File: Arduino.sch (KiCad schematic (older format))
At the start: 16 parts

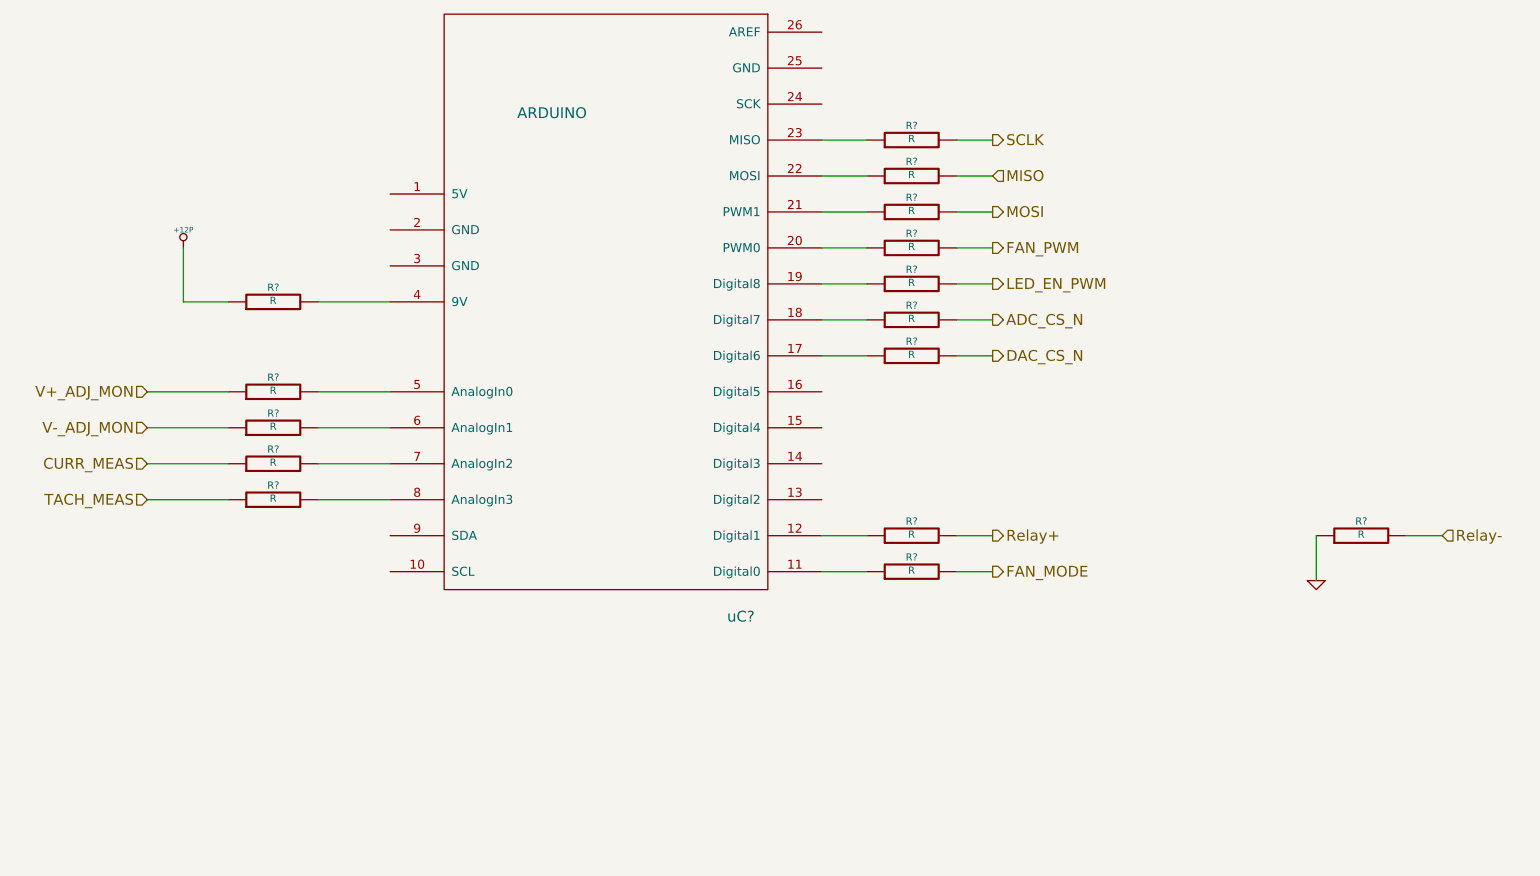
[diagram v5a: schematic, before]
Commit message: 5.3 Video 1/2 Associating and Placing the Relay Module
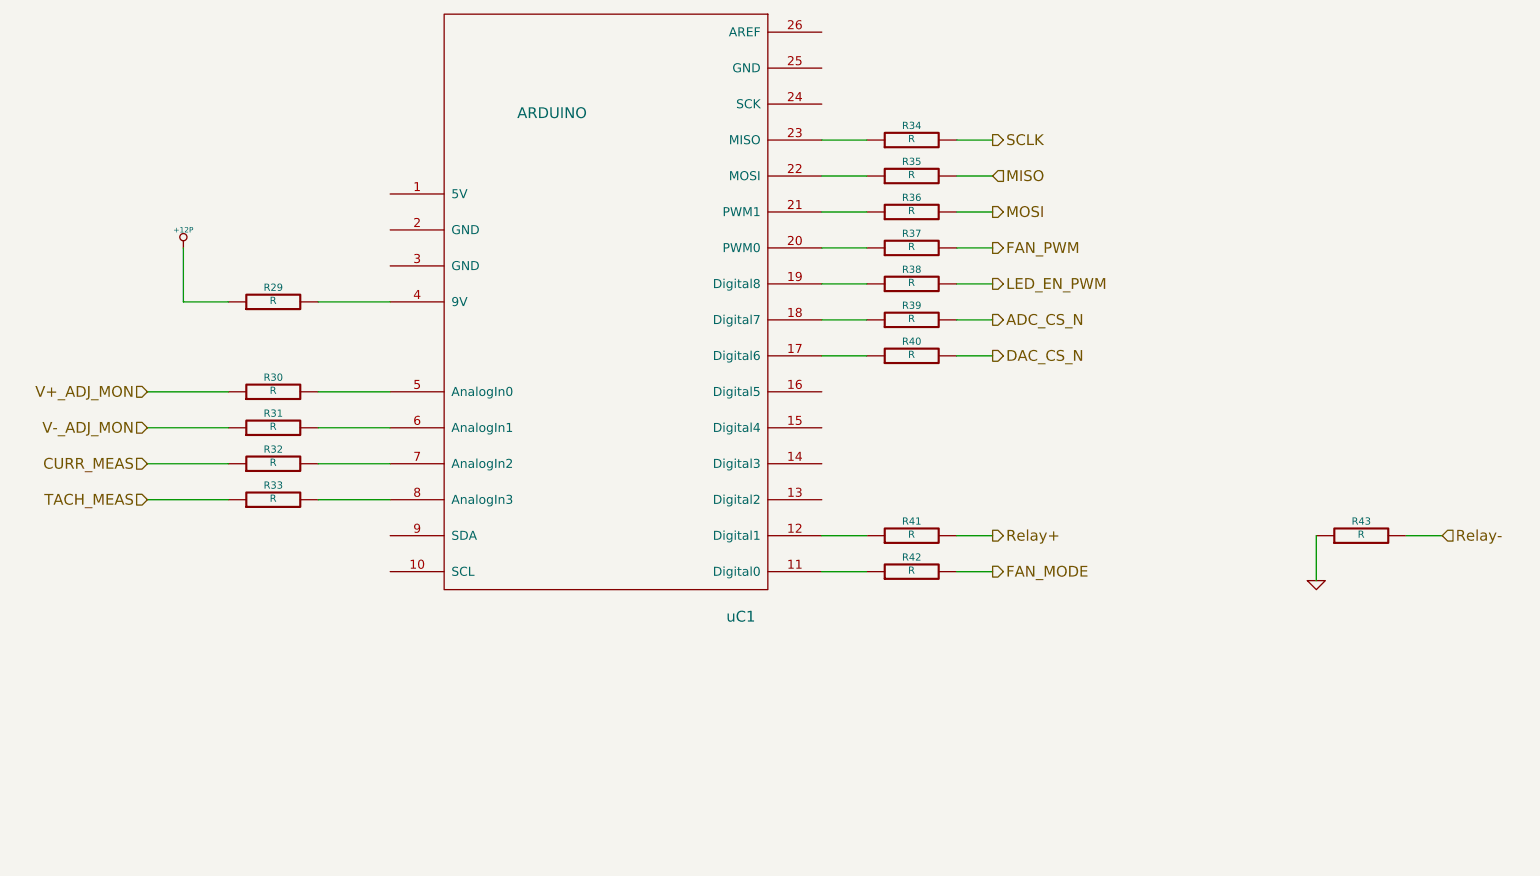
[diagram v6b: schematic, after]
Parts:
- gave numbers to parts that had none: 16
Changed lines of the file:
@@
 Sheet 9 9
 Title ""
-Date "13 feb 2014"
+Date "19 feb 2014"
 Rev ""
 Comp ""
@@
 TACH_MEAS
 $Comp
-L R R?
+L R R30
 U 1 1 52F8F2D4
 P 2100 4000
-F 0 "R?" V 2180 4000 40  0000 C CNN
+F 0 "R30" V 2180 4000 40  0000 C CNN
 F 1 "R" V 2107 4001 40  0000 C CNN
 F 2 "~" V 2030 4000 30  0000 C CNN
@@
 $EndComp
 $Comp
-L R R?
+L R R31
 U 1 1 52F8F2E1
 P 2100 4200
-F 0 "R?" V 2180 4200 40  0000 C CNN
+F 0 "R31" V 2180 4200 40  0000 C CNN
 F 1 "R" V 2107 4201 40  0000 C CNN
 F 2 "~" V 2030 4200 30  0000 C CNN
@@
 $EndComp
 $Comp
-L R R?
+L R R32
 U 1 1 52F8F2E7
 P 2100 4400
-F 0 "R?" V 2180 4400 40  0000 C CNN
+F 0 "R32" V 2180 4400 40  0000 C CNN
 F 1 "R" V 2107 4401 40  0000 C CNN
 F 2 "~" V 2030 4400 30  0000 C CNN
@@
 $EndComp
 $Comp
-L R R?
+L R R33
 U 1 1 52F8F2F7
 P 2100 4600
-F 0 "R?" V 2180 4600 40  0000 C CNN
+F 0 "R33" V 2180 4600 40  0000 C CNN
 F 1 "R" V 2107 4601 40  0000 C CNN
 F 2 "~" V 2030 4600 30  0000 C CNN
@@
 	2750 4600 2350 4600
 $Comp
-L R R?
+L R R34
 U 1 1 52F8F30B
 P 5650 2600
-F 0 "R?" V 5730 2600 40  0000 C CNN
+F 0 "R34" V 5730 2600 40  0000 C CNN
 F 1 "R" V 5657 2601 40  0000 C CNN
 F 2 "~" V 5580 2600 30  0000 C CNN
@@
 $EndComp
 $Comp
-L R R?
+L R R35
 U 1 1 52F8F318
 P 5650 2800
-F 0 "R?" V 5730 2800 40  0000 C CNN
+F 0 "R35" V 5730 2800 40  0000 C CNN
 F 1 "R" V 5657 2801 40  0000 C CNN
 F 2 "~" V 5580 2800 30  0000 C CNN
@@
 $EndComp
 $Comp
-L R R?
+L R R36
 U 1 1 52F8F31E
 P 5650 3000
-F 0 "R?" V 5730 3000 40  0000 C CNN
+F 0 "R36" V 5730 3000 40  0000 C CNN
 F 1 "R" V 5657 3001 40  0000 C CNN
 F 2 "~" V 5580 3000 30  0000 C CNN
@@
 $EndComp
 $Comp
-L R R?
+L R R39
 U 1 1 52F8F324
 P 5650 3600
-F 0 "R?" V 5730 3600 40  0000 C CNN
+F 0 "R39" V 5730 3600 40  0000 C CNN
 F 1 "R" V 5657 3601 40  0000 C CNN
 F 2 "~" V 5580 3600 30  0000 C CNN
@@
 $EndComp
 $Comp
-L R R?
+L R R41
 U 1 1 52F8F32A
 P 5650 4800
-F 0 "R?" V 5730 4800 40  0000 C CNN
+F 0 "R41" V 5730 4800 40  0000 C CNN
 F 1 "R" V 5657 4801 40  0000 C CNN
 F 2 "~" V 5580 4800 30  0000 C CNN
@@
 $EndComp
 $Comp
-L R R?
+L R R37
 U 1 1 52F8F330
 P 5650 3200
-F 0 "R?" V 5730 3200 40  0000 C CNN
+F 0 "R37" V 5730 3200 40  0000 C CNN
 F 1 "R" V 5657 3201 40  0000 C CNN
 F 2 "~" V 5580 3200 30  0000 C CNN
@@
 Relay-
 $Comp
-L GND #PWR?
+L GND #PWR048
 U 1 1 52F8F33B
 P 7900 5050
-F 0 "#PWR?" H 7900 5050 30  0001 C CNN
+F 0 "#PWR048" H 7900 5050 30  0001 C CNN
 F 1 "GND" H 7900 4980 30  0001 C CNN
 F 2 "" H 7900 5050 60  0000 C CNN
@@
 $EndComp
 $Comp
-L R R?
+L R R43
 U 1 1 52F8F34C
 P 8150 4800
-F 0 "R?" V 8230 4800 40  0000 C CNN
+F 0 "R43" V 8230 4800 40  0000 C CNN
 F 1 "R" V 8157 4801 40  0000 C CNN
 F 2 "~" V 8080 4800 30  0000 C CNN
@@
 DAC_CS_N
 $Comp
-L R R?
+L R R40
 U 1 1 52F844DD
 P 5650 3800
-F 0 "R?" V 5730 3800 40  0000 C CNN
+F 0 "R40" V 5730 3800 40  0000 C CNN
 F 1 "R" V 5657 3801 40  0000 C CNN
 F 2 "~" V 5580 3800 30  0000 C CNN
@@
 LED_EN_PWM
 $Comp
-L R R?
+L R R38
 U 1 1 52F844E8
 P 5650 3400
-F 0 "R?" V 5730 3400 40  0000 C CNN
+F 0 "R38" V 5730 3400 40  0000 C CNN
 F 1 "R" V 5657 3401 40  0000 C CNN
 F 2 "~" V 5580 3400 30  0000 C CNN
@@
 FAN_MODE
 $Comp
-L R R?
+L R R42
 U 1 1 52F897E0
 P 5650 5000
-F 0 "R?" V 5730 5000 40  0000 C CNN
+F 0 "R42" V 5730 5000 40  0000 C CNN
 F 1 "R" V 5657 5001 40  0000 C CNN
 F 2 "~" V 5580 5000 30  0000 C CNN
@@
 	5900 5000 6100 5000
 $Comp
-L R R?
+L R R29
 U 1 1 52F897E9
 P 2100 3500
-F 0 "R?" V 2180 3500 40  0000 C CNN
+F 0 "R29" V 2180 3500 40  0000 C CNN
 F 1 "R" V 2107 3501 40  0000 C CNN
 F 2 "~" V 2030 3500 30  0000 C CNN
@@
 	2750 3500 2350 3500
 $Comp
-L +12P #PWR?
+L +12P #PWR049
 U 1 1 52F8980E
 P 1600 3200
-F 0 "#PWR?" H 1600 3170 30  0001 C CNN
+F 0 "#PWR049" H 1600 3170 30  0001 C CNN
 F 1 "+12P" H 1600 3300 30  0000 C CNN
 F 2 "" H 1600 3200 60  0000 C CNN
@@
 	1600 3500 1600 3200
 $Comp
-L ARDUINO uC?
+L ARDUINO uC1
 U 1 1 52FCA476
 P 3950 4900
-F 0 "uC?" H 4700 4550 60  0000 C CNN
+F 0 "uC1" H 4700 4550 60  0000 C CNN
 F 1 "ARDUINO" H 3650 7350 60  0000 C CNN
 F 2 "~" H 3950 4900 60  0000 C CNN

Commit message: 5.4 Video 1/2 Associating and Placing the Thermocouple Module
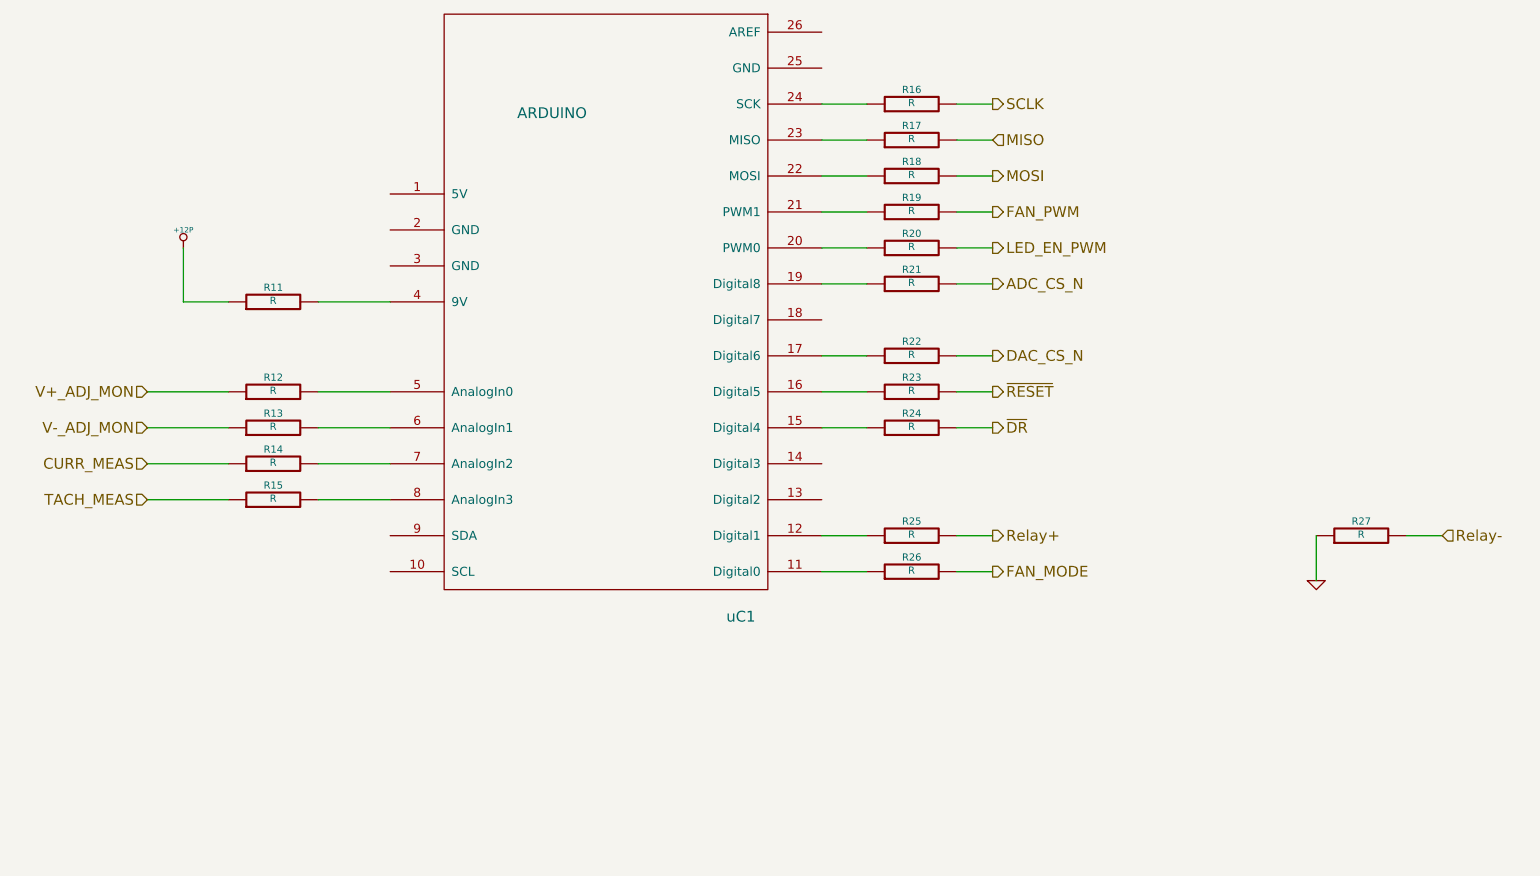
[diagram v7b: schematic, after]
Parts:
- added R23, R24: R, ~, symbol R
- renumbered R29 to R11, R30 to R12, R31 to R13, R32 to R14, R33 to R15, R34 to R16, R35 to R17, R36 to R18, R37 to R19, R38 to R20, R39 to R21, R40 to R22, R41 to R25, R42 to R26, R43 to R27
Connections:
- net at R20.1: now also uC1.20 (PWM0); no longer uC1.19 (Digital8)
- net at R16.1: now also uC1.24 (SCK); no longer uC1.23 (MISO)
- net at R17.1: now also uC1.23 (MISO); no longer uC1.22 (MOSI)
- net at R18.1: now also uC1.22 (MOSI); no longer uC1.21 (PWM1)
- net at R21.1: now also uC1.19 (Digital8); no longer uC1.18 (Digital7)
- net at R19.1: now also uC1.21 (PWM1); no longer uC1.20 (PWM0)
- net at uC1.15 (Digital4): now also R24.1
- net at uC1.16 (Digital5): now also R23.1
- new net ~DR: R24.2
- new net ~RESET: R23.2
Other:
- moved on the sheet: R16, R17, R18, R19, R20, R21
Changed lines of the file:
@@
 $Descr A4 11693 8268
 encoding utf-8
-Sheet 9 9
+Sheet 7 9
 Title ""
-Date "19 feb 2014"
+Date "21 feb 2014"
 Rev ""
 Comp ""
@@
 Text HLabel 6100 4800 2    60   Output ~ 0
 Relay+
+Text HLabel 6100 2800 2    60   Output ~ 0
+MOSI
+Text HLabel 6100 2600 2    60   Input ~ 0
+MISO
+Text HLabel 6100 2400 2    60   Output ~ 0
+SCLK
+Text HLabel 6100 3400 2    60   Output ~ 0
+ADC_CS_N
 Text HLabel 6100 3000 2    60   Output ~ 0
-MOSI
-Text HLabel 6100 2800 2    60   Input ~ 0
-MISO
-Text HLabel 6100 2600 2    60   Output ~ 0
-SCLK
-Text HLabel 6100 3600 2    60   Output ~ 0
-ADC_CS_N
-Text HLabel 6100 3200 2    60   Output ~ 0
 FAN_PWM
 Text HLabel 1400 4600 0    60   Input ~ 0
 TACH_MEAS
 $Comp
-L R R30
+L R R12
 U 1 1 52F8F2D4
 P 2100 4000
-F 0 "R30" V 2180 4000 40  0000 C CNN
+F 0 "R12" V 2180 4000 40  0000 C CNN
 F 1 "R" V 2107 4001 40  0000 C CNN
 F 2 "~" V 2030 4000 30  0000 C CNN
@@
 $EndComp
 $Comp
-L R R31
+L R R13
 U 1 1 52F8F2E1
 P 2100 4200
-F 0 "R31" V 2180 4200 40  0000 C CNN
+F 0 "R13" V 2180 4200 40  0000 C CNN
 F 1 "R" V 2107 4201 40  0000 C CNN
 F 2 "~" V 2030 4200 30  0000 C CNN
@@
 $EndComp
 $Comp
-L R R32
+L R R14
 U 1 1 52F8F2E7
 P 2100 4400
-F 0 "R32" V 2180 4400 40  0000 C CNN
+F 0 "R14" V 2180 4400 40  0000 C CNN
 F 1 "R" V 2107 4401 40  0000 C CNN
 F 2 "~" V 2030 4400 30  0000 C CNN
@@
 $EndComp
 $Comp
-L R R33
+L R R15
 U 1 1 52F8F2F7
 P 2100 4600
-F 0 "R33" V 2180 4600 40  0000 C CNN
+F 0 "R15" V 2180 4600 40  0000 C CNN
 F 1 "R" V 2107 4601 40  0000 C CNN
 F 2 "~" V 2030 4600 30  0000 C CNN
@@
 	2750 4600 2350 4600
 $Comp
-L R R34
+L R R16
 U 1 1 52F8F30B
+P 5650 2400
+F 0 "R16" V 5730 2400 40  0000 C CNN
+F 1 "R" V 5657 2401 40  0000 C CNN
+F 2 "~" V 5580 2400 30  0000 C CNN
+F 3 "~" H 5650 2400 30  0000 C CNN
+	1    5650 2400
+	0    -1   -1   0
+$EndComp
+$Comp
+L R R17
+U 1 1 52F8F318
 P 5650 2600
-F 0 "R34" V 5730 2600 40  0000 C CNN
+F 0 "R17" V 5730 2600 40  0000 C CNN
 F 1 "R" V 5657 2601 40  0000 C CNN
 F 2 "~" V 5580 2600 30  0000 C CNN
@@
 $EndComp
 $Comp
-L R R35
-U 1 1 52F8F318
+L R R18
+U 1 1 52F8F31E
 P 5650 2800
-F 0 "R35" V 5730 2800 40  0000 C CNN
+F 0 "R18" V 5730 2800 40  0000 C CNN
 F 1 "R" V 5657 2801 40  0000 C CNN
 F 2 "~" V 5580 2800 30  0000 C CNN
@@
 $EndComp
 $Comp
-L R R36
-U 1 1 52F8F31E
+L R R21
+U 1 1 52F8F324
+P 5650 3400
+F 0 "R21" V 5730 3400 40  0000 C CNN
+F 1 "R" V 5657 3401 40  0000 C CNN
+F 2 "~" V 5580 3400 30  0000 C CNN
+F 3 "~" H 5650 3400 30  0000 C CNN
+	1    5650 3400
+	0    -1   -1   0
+$EndComp
+$Comp
+L R R25
+U 1 1 52F8F32A
+P 5650 4800
+F 0 "R25" V 5730 4800 40  0000 C CNN
+F 1 "R" V 5657 4801 40  0000 C CNN
+F 2 "~" V 5580 4800 30  0000 C CNN
+F 3 "~" H 5650 4800 30  0000 C CNN
+	1    5650 4800
+	0    -1   -1   0
+$EndComp
+$Comp
+L R R19
+U 1 1 52F8F330
 P 5650 3000
-F 0 "R36" V 5730 3000 40  0000 C CNN
+F 0 "R19" V 5730 3000 40  0000 C CNN
 F 1 "R" V 5657 3001 40  0000 C CNN
 F 2 "~" V 5580 3000 30  0000 C CNN
@@
 	0    -1   -1   0
 $EndComp
-$Comp
-L R R39
-U 1 1 52F8F324
-P 5650 3600
-F 0 "R39" V 5730 3600 40  0000 C CNN
-F 1 "R" V 5657 3601 40  0000 C CNN
-F 2 "~" V 5580 3600 30  0000 C CNN
-F 3 "~" H 5650 3600 30  0000 C CNN
-	1    5650 3600
-	0    -1   -1   0
-$EndComp
-$Comp
-L R R41
-U 1 1 52F8F32A
-P 5650 4800
-F 0 "R41" V 5730 4800 40  0000 C CNN
-F 1 "R" V 5657 4801 40  0000 C CNN
-F 2 "~" V 5580 4800 30  0000 C CNN
-F 3 "~" H 5650 4800 30  0000 C CNN
-	1    5650 4800
-	0    -1   -1   0
-$EndComp
-$Comp
-L R R37
-U 1 1 52F8F330
-P 5650 3200
-F 0 "R37" V 5730 3200 40  0000 C CNN
-F 1 "R" V 5657 3201 40  0000 C CNN
-F 2 "~" V 5580 3200 30  0000 C CNN
-F 3 "~" H 5650 3200 30  0000 C CNN
-	1    5650 3200
-	0    -1   -1   0
-$EndComp
 Text HLabel 8600 4800 2    60   Input ~ 0
 Relay-
 $Comp
-L GND #PWR048
+L GND #PWR26
 U 1 1 52F8F33B
 P 7900 5050
-F 0 "#PWR048" H 7900 5050 30  0001 C CNN
+F 0 "#PWR26" H 7900 5050 30  0001 C CNN
 F 1 "GND" H 7900 4980 30  0001 C CNN
 F 2 "" H 7900 5050 60  0000 C CNN
@@
 $EndComp
 $Comp
-L R R43
+L R R27
 U 1 1 52F8F34C
 P 8150 4800
-F 0 "R43" V 8230 4800 40  0000 C CNN
+F 0 "R27" V 8230 4800 40  0000 C CNN
 F 1 "R" V 8157 4801 40  0000 C CNN
 F 2 "~" V 8080 4800 30  0000 C CNN
@@
 	1400 4600 1850 4600
 Wire Wire Line
-	5150 2600 5400 2600
-Wire Wire Line
-	5400 2800 5150 2800
-Wire Wire Line
-	5150 3000 5400 3000
-Wire Wire Line
-	5400 3600 5150 3600
+	5150 2400 5400 2400
+Wire Wire Line
+	5400 2600 5150 2600
+Wire Wire Line
+	5150 2800 5400 2800
+Wire Wire Line
+	5400 3400 5150 3400
+Wire Wire Line
+	5900 2400 6100 2400
 Wire Wire Line
 	5900 2600 6100 2600
@@
 	5900 2800 6100 2800
 Wire Wire Line
+	5900 3400 6100 3400
+Wire Wire Line
+	5150 4800 5400 4800
+Wire Wire Line
+	5400 3000 5150 3000
+Wire Wire Line
+	5900 4800 6100 4800
+Wire Wire Line
 	5900 3000 6100 3000
-Wire Wire Line
-	5900 3600 6100 3600
-Wire Wire Line
-	5150 4800 5400 4800
-Wire Wire Line
-	5400 3200 5150 3200
-Wire Wire Line
-	5900 4800 6100 4800
-Wire Wire Line
-	5900 3200 6100 3200
 Text HLabel 6100 3800 2    60   Output ~ 0
 DAC_CS_N
 $Comp
-L R R40
+L R R22
 U 1 1 52F844DD
 P 5650 3800
-F 0 "R40" V 5730 3800 40  0000 C CNN
+F 0 "R22" V 5730 3800 40  0000 C CNN
 F 1 "R" V 5657 3801 40  0000 C CNN
 F 2 "~" V 5580 3800 30  0000 C CNN
@@
 Wire Wire Line
 	5900 3800 6100 3800
-Text HLabel 6100 3400 2    60   Output ~ 0
+Text HLabel 6100 3200 2    60   Output ~ 0
 LED_EN_PWM
 $Comp
-L R R38
+L R R20
 U 1 1 52F844E8
-P 5650 3400
-F 0 "R38" V 5730 3400 40  0000 C CNN
-F 1 "R" V 5657 3401 40  0000 C CNN
-F 2 "~" V 5580 3400 30  0000 C CNN
-F 3 "~" H 5650 3400 30  0000 C CNN
-	1    5650 3400
-	0    -1   -1   0
-$EndComp
-Wire Wire Line
-	5400 3400 5150 3400
-Wire Wire Line
-	5900 3400 6100 3400
+P 5650 3200
+F 0 "R20" V 5730 3200 40  0000 C CNN
+F 1 "R" V 5657 3201 40  0000 C CNN
+F 2 "~" V 5580 3200 30  0000 C CNN
+F 3 "~" H 5650 3200 30  0000 C CNN
+	1    5650 3200
+	0    -1   -1   0
+$EndComp
+Wire Wire Line
+	5400 3200 5150 3200
+Wire Wire Line
+	5900 3200 6100 3200
 Text HLabel 6100 5000 2    60   Output ~ 0
 FAN_MODE
 $Comp
-L R R42
+L R R26
 U 1 1 52F897E0
 P 5650 5000
-F 0 "R42" V 5730 5000 40  0000 C CNN
+F 0 "R26" V 5730 5000 40  0000 C CNN
 F 1 "R" V 5657 5001 40  0000 C CNN
 F 2 "~" V 5580 5000 30  0000 C CNN
@@
 	5900 5000 6100 5000
 $Comp
-L R R29
+L R R11
 U 1 1 52F897E9
 P 2100 3500
-F 0 "R29" V 2180 3500 40  0000 C CNN
+F 0 "R11" V 2180 3500 40  0000 C CNN
 F 1 "R" V 2107 3501 40  0000 C CNN
 F 2 "~" V 2030 3500 30  0000 C CNN
@@
 	2750 3500 2350 3500
 $Comp
-L +12P #PWR049
+L +12P #PWR25
 U 1 1 52F8980E
 P 1600 3200
-F 0 "#PWR049" H 1600 3170 30  0001 C CNN
+F 0 "#PWR25" H 1600 3170 30  0001 C CNN
 F 1 "+12P" H 1600 3300 30  0000 C CNN
 F 2 "" H 1600 3200 60  0000 C CNN
@@
 	1    0    0    -1
 $EndComp
+Text HLabel 6100 4200 2    60   Output ~ 0
+~DR
+$Comp
+L R R24
+U 1 1 530707BD
+P 5650 4200
+F 0 "R24" V 5730 4200 40  0000 C CNN
+F 1 "R" V 5657 4201 40  0000 C CNN
+F 2 "~" V 5580 4200 30  0000 C CNN
+F 3 "~" H 5650 4200 30  0000 C CNN
+	1    5650 4200
+	0    -1   -1   0
+$EndComp
+Wire Wire Line
+	5400 4200 5150 4200
+Wire Wire Line
+	5900 4200 6100 4200
+Text HLabel 6100 4000 2    60   Output ~ 0
+~RESET
+$Comp
+L R R23
+U 1 1 530707C6
+P 5650 4000
+F 0 "R23" V 5730 4000 40  0000 C CNN
+F 1 "R" V 5657 4001 40  0000 C CNN
+F 2 "~" V 5580 4000 30  0000 C CNN
+F 3 "~" H 5650 4000 30  0000 C CNN
+	1    5650 4000
+	0    -1   -1   0
+$EndComp
+Wire Wire Line
+	5900 4000 6100 4000
+Wire Wire Line
+	5400 4000 5150 4000
 $EndSCHEMATC
